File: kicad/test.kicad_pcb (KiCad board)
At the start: 2 copper layers, 8 parts, among them SW10 SW_Push_Dual, SW11 SW_Push_Dual, SW12 SW_Push_Dual, SW9 SW_Push_Dual, U2 ESP32-S3-WROOM-1

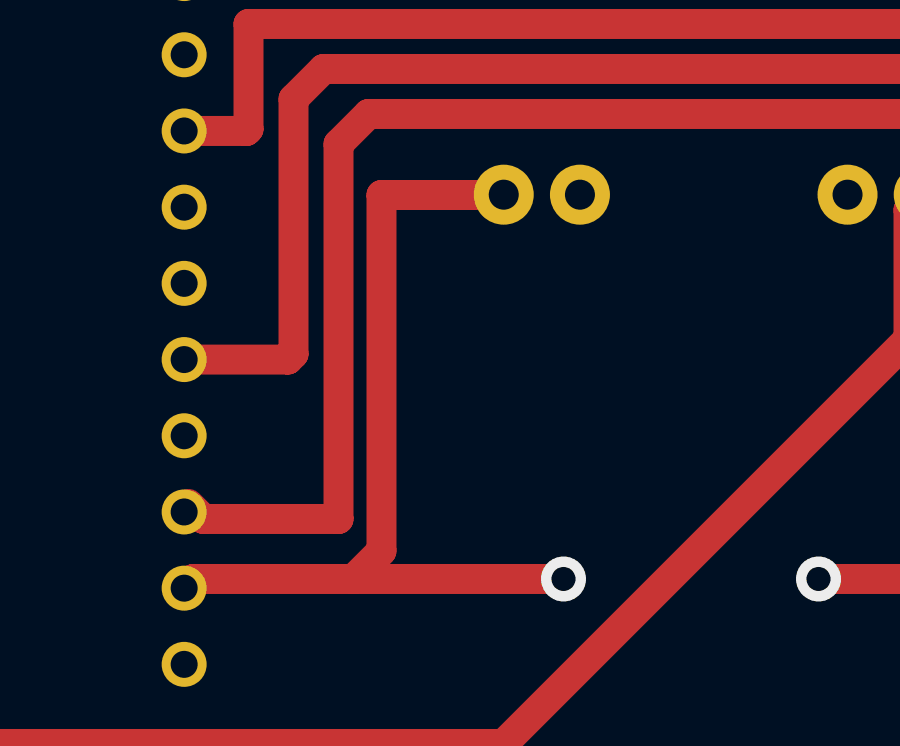
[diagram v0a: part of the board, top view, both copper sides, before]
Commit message: update scheme; add gnd tp4056 button
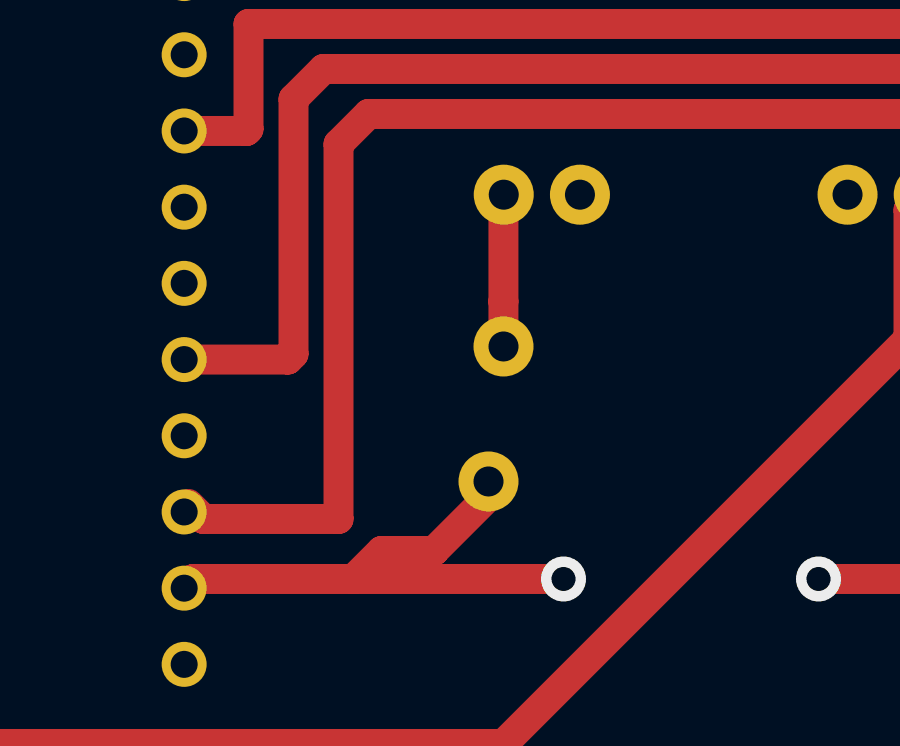
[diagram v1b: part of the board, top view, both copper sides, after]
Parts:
- added ?: , , F.Cu at (94.1, 28.0)
- added ?: , , F.Cu at (93.6, 32.5)
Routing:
- net Net-(U2-D14): track 104.2 -> 97.7 mm
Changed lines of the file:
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@@
+		(embedded_fonts no)
+	)
+	(footprint ""
+		(layer "F.Cu")
+		(at 94.07 28)
+		(property "Reference" ""
+			(at 0 0 0)
+			(layer "F.SilkS")
+			(effects
+				(font
+					(size 1.27 1.27)
+					(thickness 0.15)
+				)
+			)
+		)
+		(property "Value" ""
+			(at 0 0 0)
+			(layer "F.Fab")
+			(effects
+				(font
+					(size 1.27 1.27)
+					(thickness 0.15)
+				)
+			)
+		)
+		(property "Datasheet" ""
+			(at 0 0 0)
+			(layer "F.Fab")
+			(hide yes)
+			(effects
+				(font
+					(size 1.27 1.27)
+					(thickness 0.15)
+				)
+			)
+		)
+		(property "Description" ""
+			(at 0 0 0)
+			(layer "F.Fab")
+			(hide yes)
+			(effects
+				(font
+					(size 1.27 1.27)
+					(thickness 0.15)
+				)
+			)
+		)
+		(pad "4" thru_hole circle
+			(at 0 0 90)
+			(size 2 2)
+			(drill 1)
+			(layers "*.Cu" "*.Mask")
+			(remove_unused_layers no)
+		)
+		(embedded_fonts no)
+	)
+	(footprint ""
+		(layer "F.Cu")
+		(at 93.57 32.5)
+		(property "Reference" ""
+			(at 0 0 0)
+			(layer "F.SilkS")
+			(effects
+				(font
+					(size 1.27 1.27)
+					(thickness 0.15)
+				)
+			)
+		)
+		(property "Value" ""
+			(at 0 0 0)
+			(layer "F.Fab")
+			(effects
+				(font
+					(size 1.27 1.27)
+					(thickness 0.15)
+				)
+			)
+		)
+		(property "Datasheet" ""
+			(at 0 0 0)
+			(layer "F.Fab")
+			(hide yes)
+			(effects
+				(font
+					(size 1.27 1.27)
+					(thickness 0.15)
+				)
+			)
+		)
+		(property "Description" ""
+			(at 0 0 0)
+			(layer "F.Fab")
+			(hide yes)
+			(effects
+				(font
+					(size 1.27 1.27)
+					(thickness 0.15)
+				)
+			)
+		)
+		(pad "4" thru_hole circle
+			(at 0 0 90)
+			(size 2 2)
+			(drill 1)
+			(layers "*.Cu" "*.Mask")
+			(remove_unused_layers no)
+		)
 		(embedded_fonts no)
 	)
@@
 	)
 	(segment
-		(start 90.002807 22.950647)
-		(end 90.002807 34.817193)
+		(start 94.067391 26.502609)
+		(end 94.067391 27.997391)
 		(width 1)
 		(layer "F.Cu")
@@
 	)
 	(segment
-		(start 94.067391 22.950647)
-		(end 90.002807 22.950647)
-		(width 1)
-		(layer "F.Cu")
-		(net 8)
-	)
-	(segment
 		(start 94.078019 22.940019)
 		(end 94.067391 22.950647)
@@
 	)
 	(segment
+		(start 94.067391 26.502609)
+		(end 94.067391 22.950647)
+		(width 1)
+		(layer "F.Cu")
+		(net 8)
+	)
+	(segment
 		(start 44.07 1.25)
 		(end 44.07 10.25)
@@
 	)
 	(segment
+		(start 91.752807 34.817193)
+		(end 93.57 33)
+		(width 1)
+		(layer "F.Cu")
+		(net 8)
+	)
+	(segment
+		(start 90.002807 34.817193)
+		(end 91.752807 34.817193)
+		(width 1)
+		(layer "F.Cu")
+		(net 8)
+	)
+	(segment
 		(start 60.77 5.55)
 		(end 61.07 5.25)
@@
 		(width 1)
 		(layer "F.Cu")
+		(net 8)
+	)
+	(segment
+		(start 94.067391 27.997391)
+		(end 94.07 28)
+		(width 1)
+		(layer "F.Cu")

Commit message: slim version
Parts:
- removed ? (x2): , 
- U2: footprint My:ESP32-Wroom-32 -> RF_Module:ESP32-WROOM-32E
- moved U2 28.3 mm to (63.8, 23.5), turned to 0 degrees
- moved D1 15.1 mm to (81.6, 38.0)
- moved SW5pin1 14.6 mm to (107.1, 20.2)
- moved D2 5.93 mm to (48.1, 27.3)
- moved SW10 4.64 mm to (6.07, 9.21)
- moved SW12 4.64 mm to (6.07, 23.2)
- moved SW11 4.64 mm to (21.6, 29.7)
- moved SW9 4.64 mm to (21.6, 15.7)
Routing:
- net (no net): track 75.0 -> 303.6 mm, vias 1 -> 22
- net Net-(U2-D16): track 189.5 -> 39.4 mm, vias 3 -> 1
- net Net-(U2-D25): track 138.3 -> 18.1 mm
- net Net-(U2-D21): track 142.6 -> 54.0 mm, vias 5 -> 1
- net Net-(U2-D14): track 97.7 -> 29.0 mm
- net Net-(U2-D32): track 47.8 -> 2.22 mm, vias 0 -> 1
- net Net-(U2-D19): track 20.6 -> 50.6 mm, vias 0 -> 1
- net Net-(U2-D17): track 52.8 -> 43.4 mm, vias 0 -> 1
- net unconnected-(U2-D26-Pad26): track 9.42 -> 0.00 mm, vias 1 -> 0
- net Net-(U2-D22): track 48.9 -> 39.7 mm, vias 2 -> 1
- net Net-(D1-ESP-): track 206.4 -> 200.4 mm, vias 4 -> 2
- net Net-(D2-6_SDI_MOSI): track 2.52 -> 0.00 mm, vias 1 -> 0
- net Net-(U2-D13): track 23.7 -> 22.3 mm

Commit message: update plate
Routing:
- net (no net): track 303.6 -> 432.1 mm

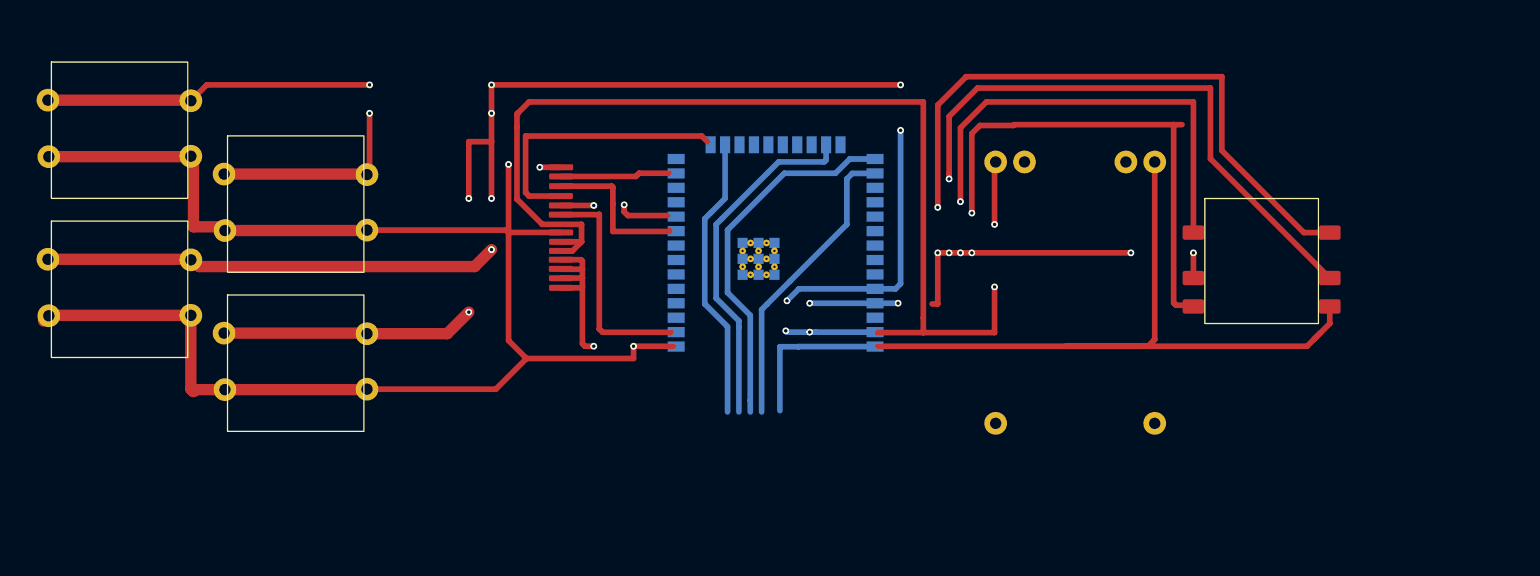
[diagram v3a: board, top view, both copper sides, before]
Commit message: update kicad plate
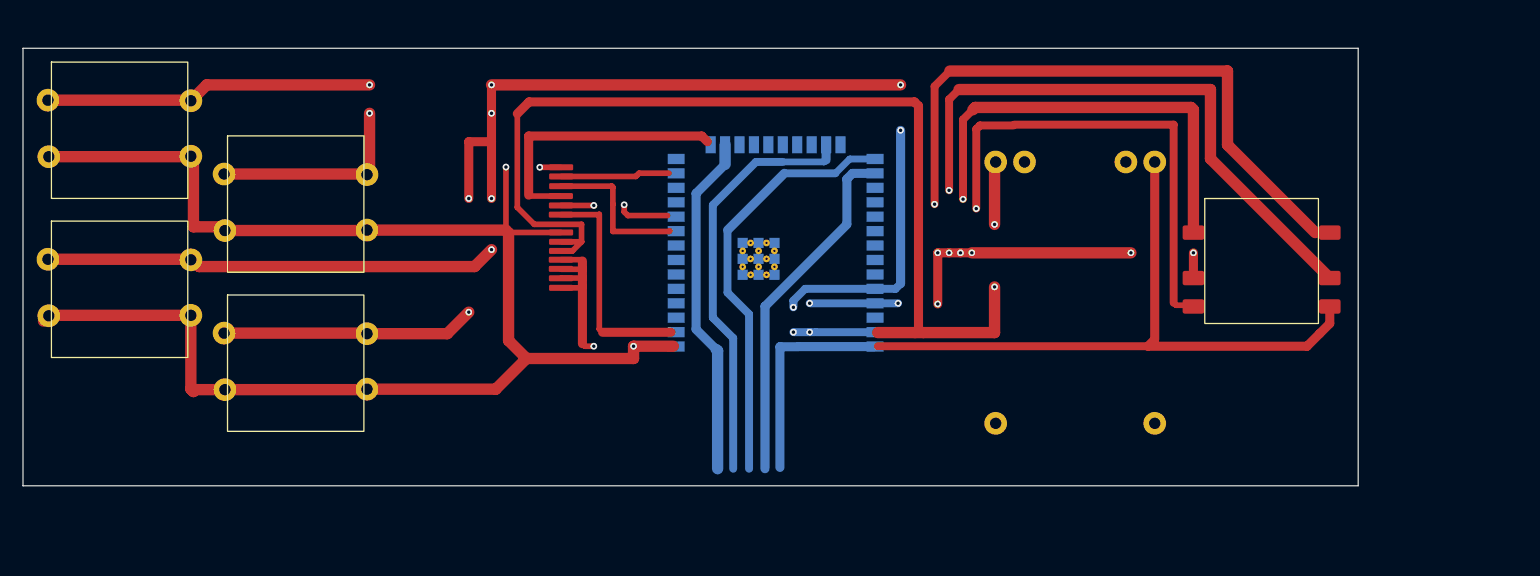
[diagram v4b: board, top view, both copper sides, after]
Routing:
- net (no net): track 432.1 -> 456.6 mm, vias 22 -> 23
- net Net-(U2-D19): track 50.6 -> 52.3 mm
- net Net-(U2-D21): track 54.0 -> 55.4 mm
- net Net-(U2-D17): track 43.4 -> 42.1 mm
- net Net-(U2-D16): track 39.4 -> 38.6 mm
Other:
- board outline added: 117.5 x 38.5 mm

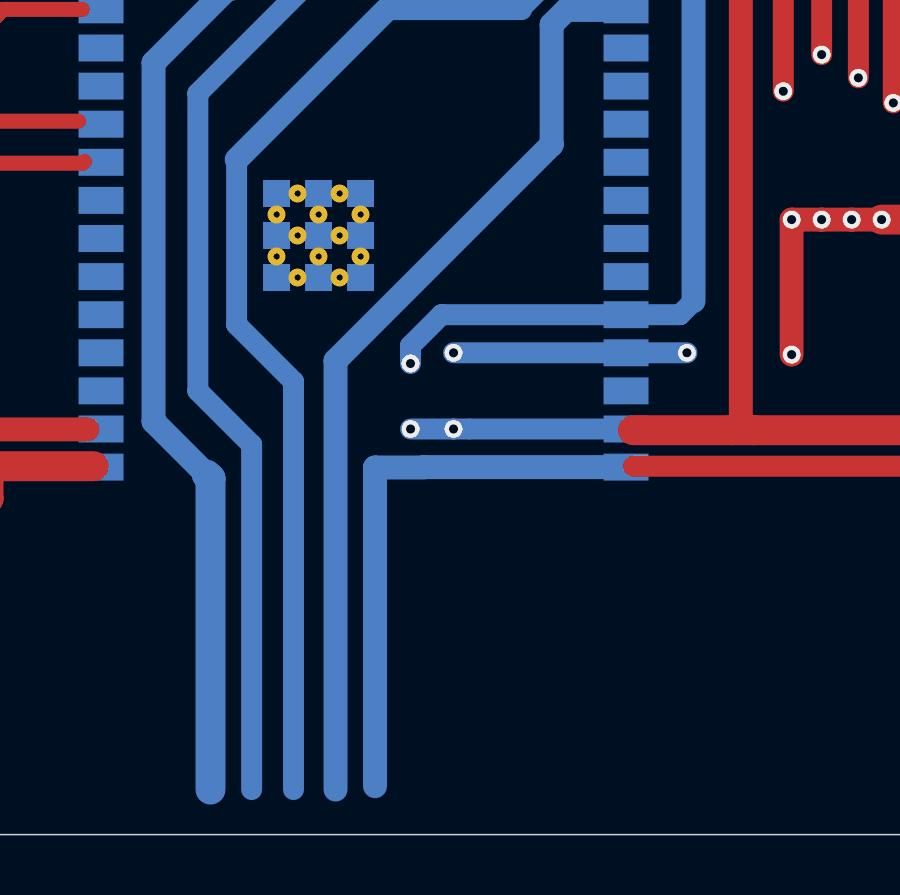
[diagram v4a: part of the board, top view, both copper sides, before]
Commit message: fix plate
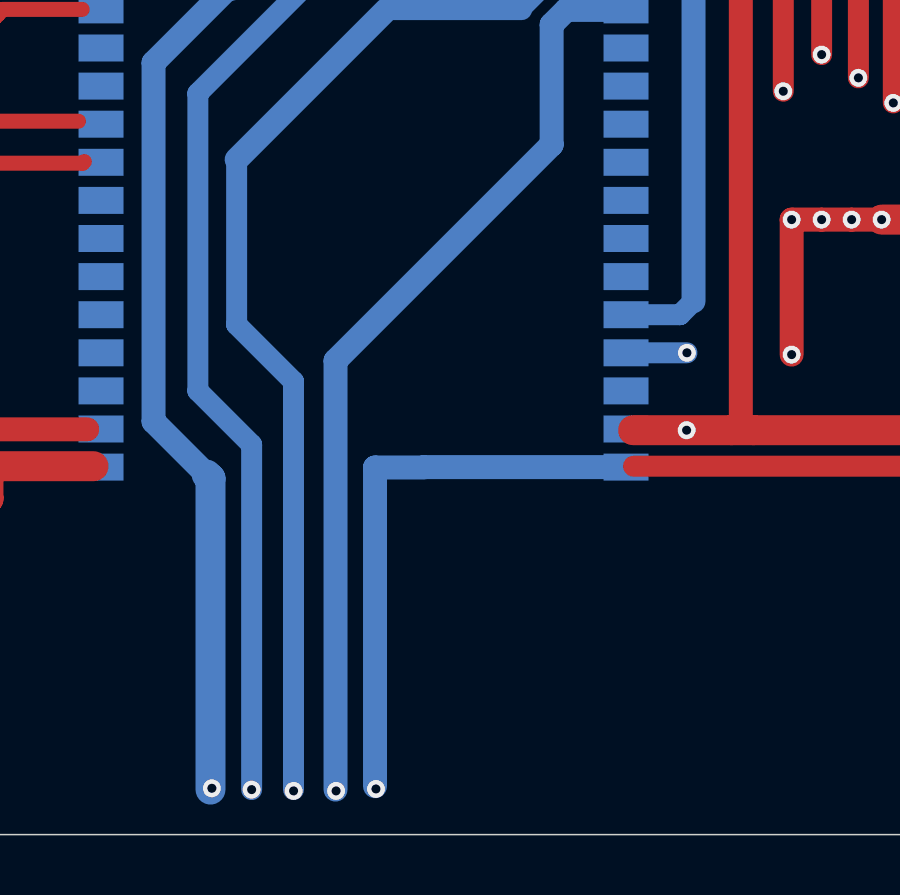
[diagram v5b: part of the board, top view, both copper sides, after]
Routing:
- net (no net): track 456.6 -> 281.4 mm, vias 23 -> 20
- net Net-(D1-ESP-): track 200.3 -> 355.1 mm, vias 2 -> 7

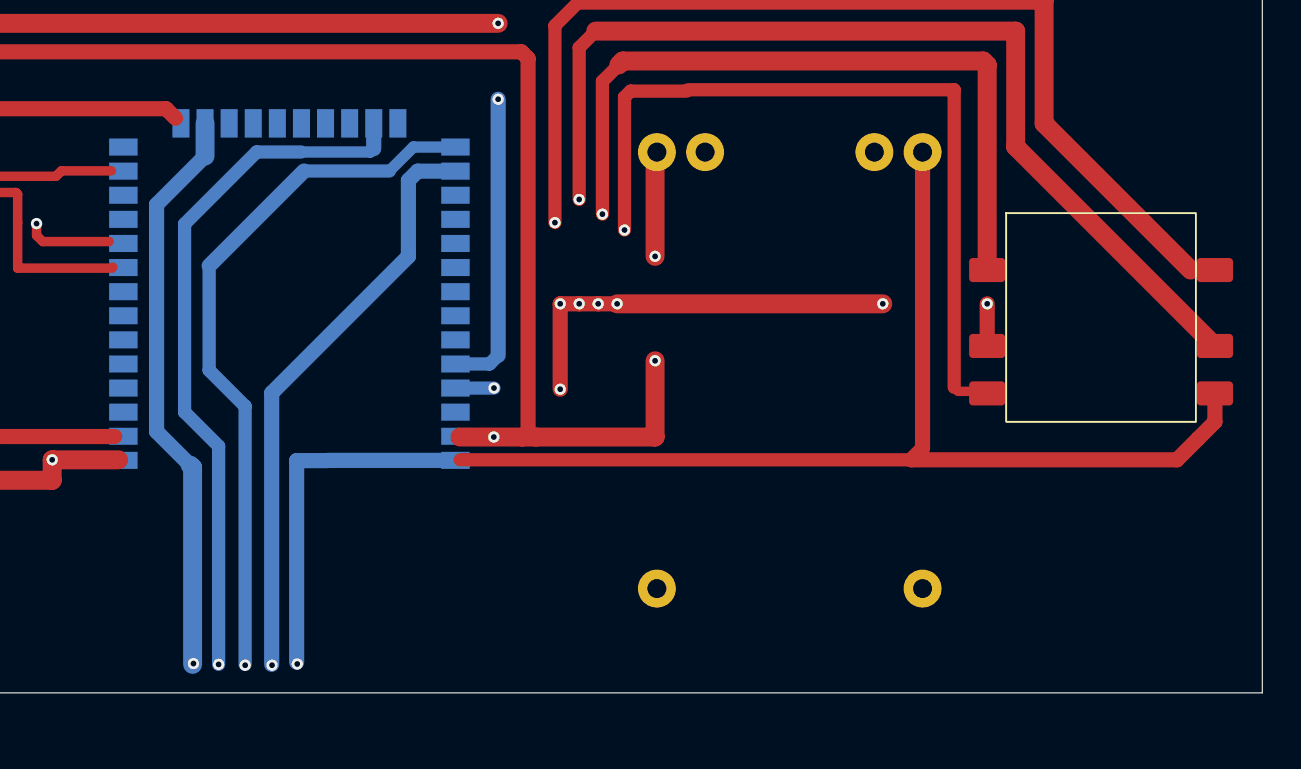
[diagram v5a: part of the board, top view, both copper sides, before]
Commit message: update kicad scheme version. Add EN to 3V3 drill and jtag change to uart
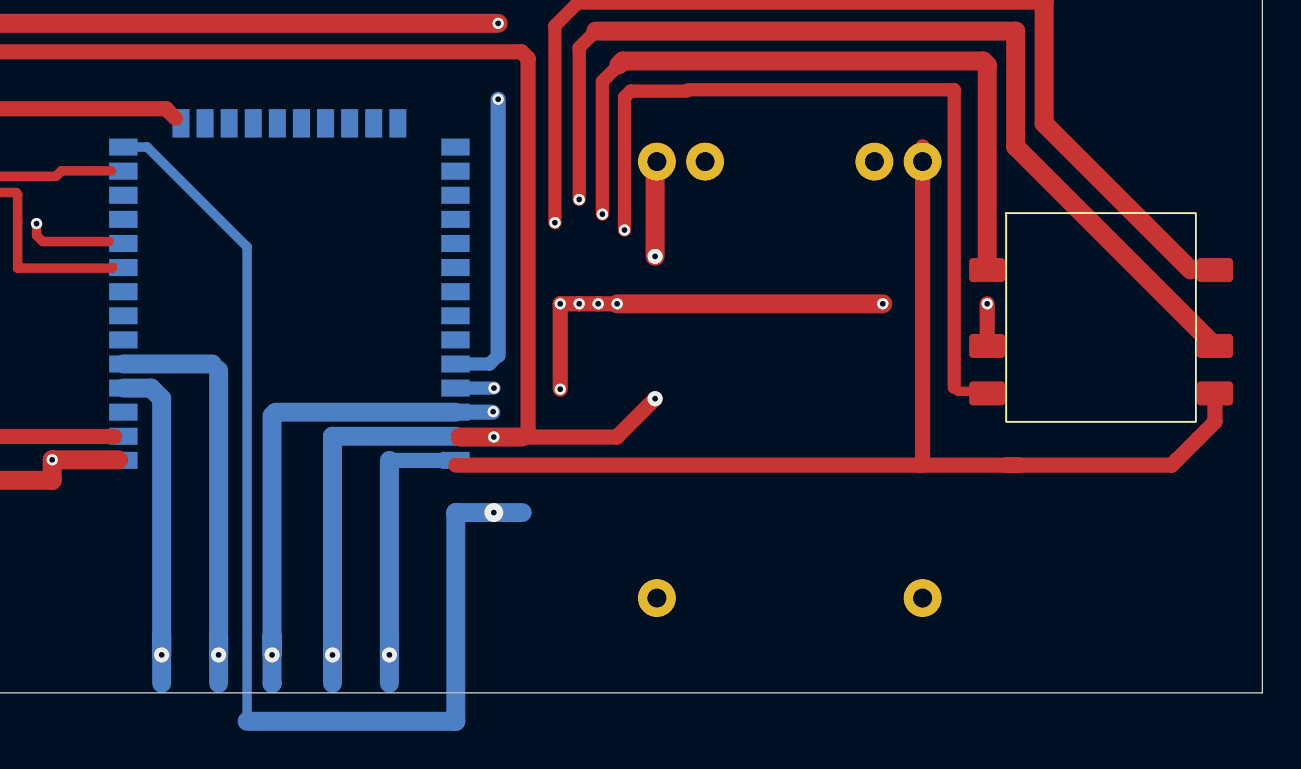
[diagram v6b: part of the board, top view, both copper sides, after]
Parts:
- moved D1 0.50 mm to (81.6, 38.5)
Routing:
- net (no net): track 281.4 -> 278.2 mm
- net Net-(D1-ESP-): track 355.1 -> 357.4 mm, vias 7 -> 9
